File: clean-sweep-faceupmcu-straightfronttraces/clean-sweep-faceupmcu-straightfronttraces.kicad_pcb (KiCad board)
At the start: 2 copper layers, 107.2 x 86.9 mm, 25 parts, among them J1 TRRS, SW1 SW_Push, SW10 SW_Push, SW11 SW_Push, SW12 SW_Push, SW13 SW_Push, SW14 SW_Push, SW15 SW_Push, SW16 SW_Push, SW17 SW_Push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

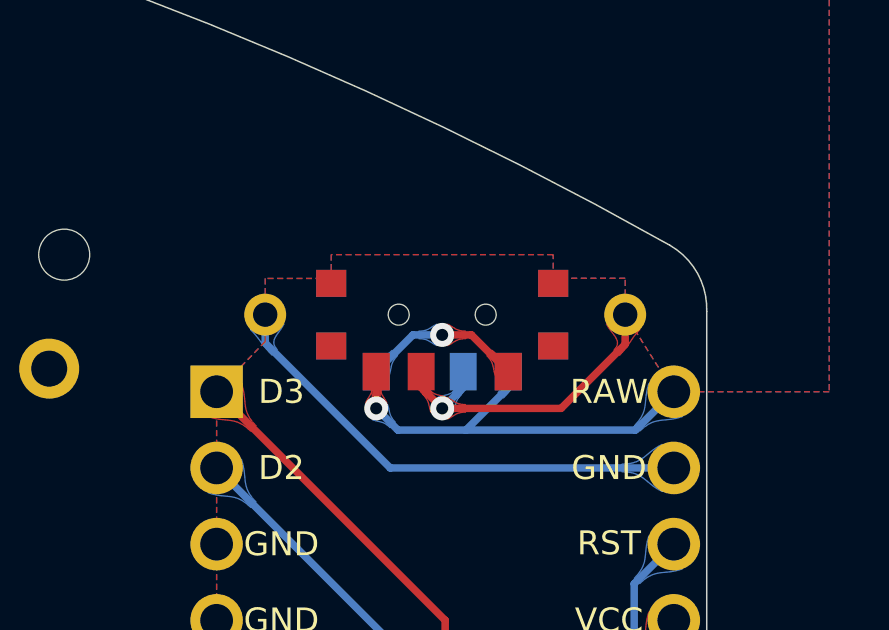
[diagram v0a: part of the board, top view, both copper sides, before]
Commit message: Add silkscreen labels to battery connection pads
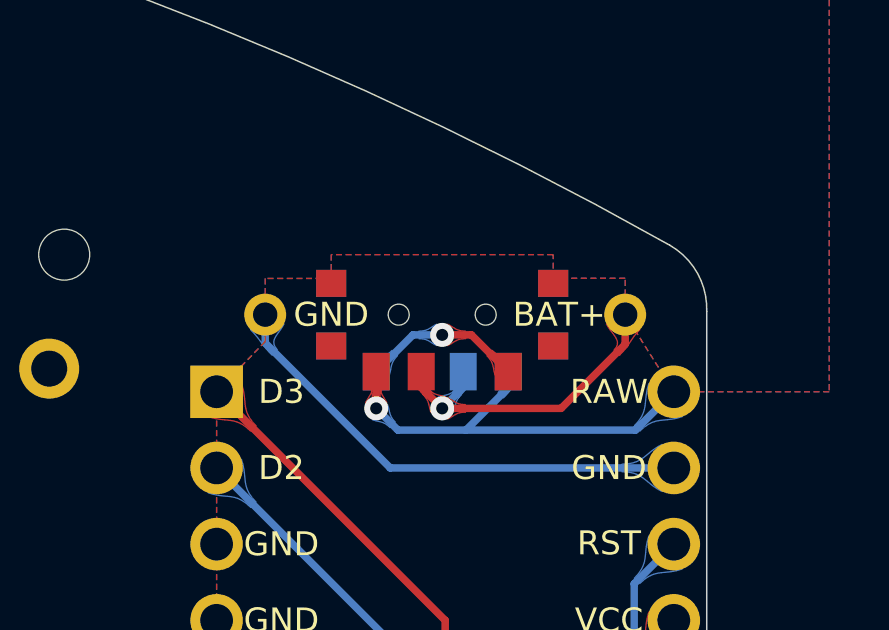
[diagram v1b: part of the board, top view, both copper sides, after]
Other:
- board text added: "BAT+"
- board text added: "GND"
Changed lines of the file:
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@@
   (gr_line (start 20.749412 86.805206) (end 20.749412 38.610478) (layer "Edge.Cuts") (width 0.05))
   (gr_line (start 115.675412 104.969838) (end 127.064092 84.811883) (layer "Edge.Cuts") (width 0.05))
+  (gr_text "GND" (at 115.4 38) (layer "B.SilkS")
+    (effects (font (size 0.8 0.8) (thickness 0.15)) (justify mirror))
+  )
+  (gr_text "BAT+" (at 123 38) (layer "B.SilkS")
+    (effects (font (size 0.8 0.8) (thickness 0.15)) (justify mirror))
+  )
+  (gr_text "GND" (at 115.4 38) (layer "F.SilkS")
+    (effects (font (size 0.8 0.8) (thickness 0.15)))
+  )
+  (gr_text "BAT+" (at 123 38) (layer "F.SilkS")
+    (effects (font (size 0.8 0.8) (thickness 0.15)))
+  )
   (segment (start 123.063326 41.124502) (end 125.2 38.987828) (width 0.25) (layer "F.Cu") (net 1))
   (segment (start 119.1 41.124502) (end 123.063326 41.124502) (width 0.25) (layer "F.Cu") (net 1))
